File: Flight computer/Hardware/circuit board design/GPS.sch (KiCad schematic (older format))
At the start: 5 parts, among them J6 Conn_Coaxial, U4 MAX-M8C

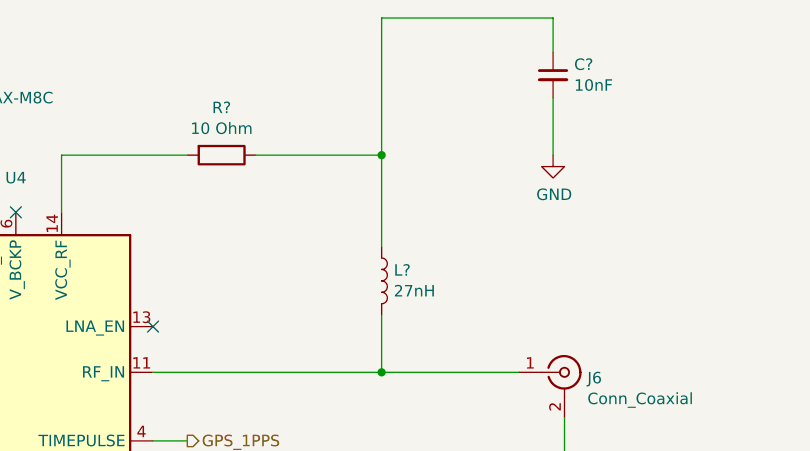
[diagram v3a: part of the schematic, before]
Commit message: fixed erc problems with Johanson integrated Frontend.
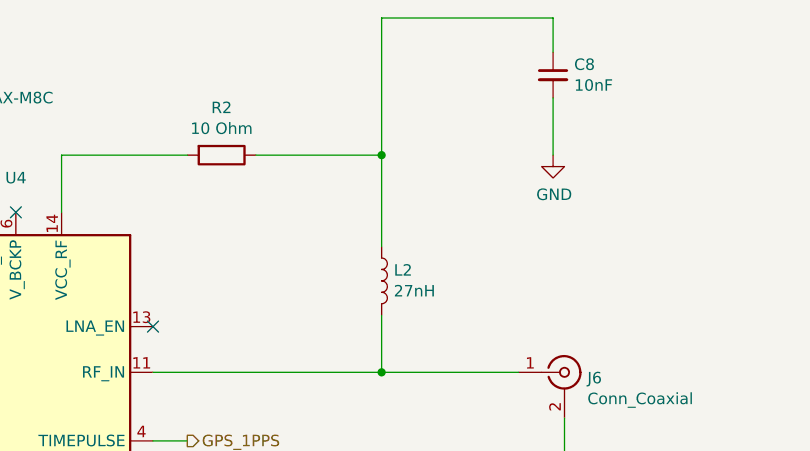
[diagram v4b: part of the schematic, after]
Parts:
- gave numbers to parts that had none: 3
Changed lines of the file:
@@
 	8450 4800 8450 4250
 $Comp
-L power:GND #PWR?
+L power:GND #PWR0114
 U 1 1 5D7B7248
 P 8450 4800
-F 0 "#PWR?" H 8450 4550 50  0001 C CNN
+F 0 "#PWR0114" H 8450 4550 50  0001 C CNN
 F 1 "GND" H 8455 4627 50  0000 C CNN
 F 2 "" H 8450 4800 50  0001 C CNN
@@
 	7650 4050 8250 4050
 $Comp
-L Device:L L?
+L Device:L L2
 U 1 1 5D7B7FB8
 P 7650 3650
-F 0 "L?" H 7703 3696 50  0000 L CNN
+F 0 "L2" H 7703 3696 50  0000 L CNN
 F 1 "27nH" H 7703 3605 50  0000 L CNN
 F 2 "" H 7650 3650 50  0001 C CNN
@@
 	7650 3100 7650 3500
 $Comp
-L Device:R R?
+L Device:R R2
 U 1 1 5D7B91DB
 P 6950 3100
-F 0 "R?" V 6743 3100 50  0000 C CNN
+F 0 "R2" V 6743 3100 50  0000 C CNN
 F 1 "10 Ohm" V 6834 3100 50  0000 C CNN
 F 2 "" V 6880 3100 50  0001 C CNN
@@
 Connection ~ 7650 3100
 $Comp
-L power:GND #PWR?
+L power:GND #PWR0116
 U 1 1 5D7B9CCD
 P 8400 3100
-F 0 "#PWR?" H 8400 2850 50  0001 C CNN
+F 0 "#PWR0116" H 8400 2850 50  0001 C CNN
 F 1 "GND" H 8405 2927 50  0000 C CNN
 F 2 "" H 8400 3100 50  0001 C CNN
@@
 	7650 2500 8400 2500
 $Comp
-L Device:C_Small C?
+L Device:C_Small C8
 U 1 1 5D7BADC4
 P 8400 2750
-F 0 "C?" H 8492 2796 50  0000 L CNN
+F 0 "C8" H 8492 2796 50  0000 L CNN
 F 1 "10nF" H 8492 2705 50  0000 L CNN
 F 2 "" H 8400 2750 50  0001 C CNN

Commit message: added in some comments
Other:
- note added: "Arrangement for Active antenna\n"
- note added: "Connected to active antenna, likely 2066400001 \nMolex active antenna. UFL connector\n"
- note removed: "Arranged according to Figure 7 in the MAX-8 / MAX-M8 u-blox 8 / M8 GNSS modules Hardware Integration Manual. Page 12."
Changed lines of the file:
@@
 Sheet 3 7
 Title ""
-Date ""
-Rev ""
-Comp ""
+Date "2019-09-09"
+Rev "1.0"
+Comp "Imperial College Space Society"
 Comment1 ""
 Comment2 ""
@@
 GPS_1PPS
 Text Notes 3000 5800 0    50   ~ 0
-Arranged according to Figure 7 in the MAX-8 / MAX-M8 u-blox 8 / M8 GNSS modules Hardware Integration Manual. Page 12.
-Text Notes 7550 5250 0    50   ~ 0
+Arrangement for Active antenna\n
+Text Notes 3800 6200 0    50   ~ 0
 http://www.explorelabs.com/blog/designing-a-gps-receiver/#ref-ublox-datasheet\n\nImportant info on why we use the components\n
 $Comp
@@
 Wire Wire Line
 	8400 2850 8400 3100
+Text Notes 8200 3850 0    50   ~ 0
+Connected to active antenna, likely 2066400001 \nMolex active antenna. UFL connector\n
 $EndSCHEMATC

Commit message: completed the pi circuit for Telemetry antenna
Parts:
- C8: footprint (none) -> Capacitor_SMD:C_0402_1005Metric
- L2, R2: footprint (none) -> Resistor_SMD:R_0402_1005Metric
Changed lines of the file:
@@
 F 0 "L2" H 7703 3696 50  0000 L CNN
 F 1 "27nH" H 7703 3605 50  0000 L CNN
-F 2 "" H 7650 3650 50  0001 C CNN
+F 2 "Resistor_SMD:R_0402_1005Metric" H 7650 3650 50  0001 C CNN
 F 3 "~" H 7650 3650 50  0001 C CNN
 	1    7650 3650
@@
 F 0 "R2" V 6743 3100 50  0000 C CNN
 F 1 "10 Ohm" V 6834 3100 50  0000 C CNN
-F 2 "" V 6880 3100 50  0001 C CNN
+F 2 "Resistor_SMD:R_0402_1005Metric" V 6880 3100 50  0001 C CNN
 F 3 "~" H 6950 3100 50  0001 C CNN
 	1    6950 3100
@@
 F 0 "C8" H 8492 2796 50  0000 L CNN
 F 1 "10nF" H 8492 2705 50  0000 L CNN
-F 2 "" H 8400 2750 50  0001 C CNN
+F 2 "Capacitor_SMD:C_0402_1005Metric" H 8400 2750 50  0001 C CNN
 F 3 "~" H 8400 2750 50  0001 C CNN
 	1    8400 2750

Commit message: added in comment about where I got the ref layout for GPS+active antenna
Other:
- note added: "Layout according to MAX-8 / MAX-M8, \nHardware Integration Manual,\nSection 2.4.2 Antenna design with active antenna."
- note removed: "Arrangement for Active antenna\n"
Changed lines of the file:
@@
 Text HLabel 6800 4350 2    50   Output ~ 0
 GPS_1PPS
-Text Notes 3000 5800 0    50   ~ 0
-Arrangement for Active antenna\n
 Text Notes 3800 6200 0    50   ~ 0
 http://www.explorelabs.com/blog/designing-a-gps-receiver/#ref-ublox-datasheet\n\nImportant info on why we use the components\n
@@
 Wire Wire Line
 	8400 2850 8400 3100
-Text Notes 8200 3850 0    50   ~ 0
+Text Notes 7500 5350 0    50   ~ 0
 Connected to active antenna, likely 2066400001 \nMolex active antenna. UFL connector\n
+Text Notes 5100 2400 0    50   ~ 0
+Layout according to MAX-8 / MAX-M8, \nHardware Integration Manual,\nSection 2.4.2 Antenna design with active antenna.
 $EndSCHEMATC

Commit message: tried routing first round
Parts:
- added C11: 100nF, Capacitor_SMD:C_0603_1608Metric, symbol Device:C_Small
- added C12: 2u2F, Capacitor_SMD:C_0603_1608Metric, symbol Device:C_Small
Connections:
- net +3V3: now also C11.1, C12.1
- net GND: now also C11.2, C12.2
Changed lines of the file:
@@
 http://www.explorelabs.com/blog/designing-a-gps-receiver/#ref-ublox-datasheet\n\nImportant info on why we use the components\n
-$Comp
-L power:+3.3V #PWR010
-U 1 1 5D692740
-P 5850 3150
-F 0 "#PWR010" H 5850 3000 50  0001 C CNN
-F 1 "+3.3V" H 5865 3323 50  0000 C CNN
-F 2 "" H 5850 3150 50  0001 C CNN
-F 3 "" H 5850 3150 50  0001 C CNN
-	1    5850 3150
-	1    0    0    -1
-$EndComp
 $Comp
 L power:GND #PWR011
@@
 	1    0    0    -1
 $EndComp
-Wire Wire Line
-	5850 3150 5850 3250
-Wire Wire Line
-	5950 3250 5850 3250
 Text HLabel 5150 3750 0    50   Output ~ 0
 GPS_TXD
@@
 Wire Wire Line
 	7650 3800 7650 4050
-Connection ~ 5850 3250
-Wire Wire Line
-	5150 4450 5450 4450
-Wire Wire Line
-	5850 3250 5850 3350
-Wire Wire Line
-	5950 3350 5950 3250
-NoConn ~ 6050 3350
-NoConn ~ 5450 4250
-Wire Wire Line
-	6650 4350 6800 4350
-Wire Wire Line
-	5450 3650 5150 3650
-Wire Wire Line
-	5150 3750 5450 3750
-Wire Wire Line
-	5450 4350 5150 4350
-Wire Wire Line
-	5150 4050 5450 4050
-Wire Wire Line
-	5450 3950 5150 3950
-NoConn ~ 6650 3850
-Wire Wire Line
-	6650 4050 7650 4050
-Wire Wire Line
-	6050 4750 6050 4900
-$Comp
-L RF_GPS:MAX-M8C U4
-U 1 1 5D610F77
-P 6050 4050
-F 0 "U4" H 6050 4900 50  0000 C CNN
-F 1 "MAX-M8C" H 6050 5250 50  0000 C CNN
-F 2 "RF_GPS:ublox_MAX" H 6450 3400 50  0001 C CNN
-F 3 "https://www.u-blox.com/sites/default/files/MAX-M8-FW3_DataSheet_%28UBX-15031506%29.pdf" H 6050 4050 50  0001 C CNN
-F 4 "11.99" H 6050 4050 50  0001 C CNN "Cost"
-F 5 "https://store.uputronics.com/index.php?route=product/product&product_id=71&search=ublox" H 6050 4050 50  0001 C CNN "Purchase link"
-	1    6050 4050
-	1    0    0    -1
-$EndComp
-Wire Wire Line
-	6250 3350 6250 3100
 Wire Wire Line
 	6250 3100 6800 3100
@@
 Text Notes 7500 5350 0    50   ~ 0
 Connected to active antenna, likely 2066400001 \nMolex active antenna. UFL connector\n
-Text Notes 5100 2400 0    50   ~ 0
+Text Notes 7000 1150 0    50   ~ 0
 Layout according to MAX-8 / MAX-M8, \nHardware Integration Manual,\nSection 2.4.2 Antenna design with active antenna.
+NoConn ~ 6050 3350
+NoConn ~ 5450 4250
+Wire Wire Line
+	6650 4350 6800 4350
+Wire Wire Line
+	6250 3350 6250 3100
+NoConn ~ 6650 3850
+Wire Wire Line
+	6650 4050 7650 4050
+Wire Wire Line
+	6050 4750 6050 4900
+Wire Wire Line
+	5950 3350 5950 2650
+Wire Wire Line
+	5850 2650 5850 3350
+Connection ~ 5850 2650
+Wire Wire Line
+	5950 2650 5850 2650
+Wire Wire Line
+	5850 2100 5850 2650
+$Comp
+L power:+3.3V #PWR010
+U 1 1 5D692740
+P 5850 2100
+F 0 "#PWR010" H 5850 1950 50  0001 C CNN
+F 1 "+3.3V" H 5865 2273 50  0000 C CNN
+F 2 "" H 5850 2100 50  0001 C CNN
+F 3 "" H 5850 2100 50  0001 C CNN
+	1    5850 2100
+	1    0    0    -1
+$EndComp
+Wire Wire Line
+	5300 3050 5300 2950
+Wire Wire Line
+	5650 2950 5650 3050
+Wire Wire Line
+	5650 2650 5300 2650
+Connection ~ 5650 2650
+Wire Wire Line
+	5650 2750 5650 2650
+Wire Wire Line
+	5300 2650 5300 2750
+Wire Wire Line
+	5850 2650 5650 2650
+$Comp
+L Device:C_Small C?
+U 1 1 5D99D571
+P 5300 2850
+AR Path="/5D5B17D8/5D99D571" Ref="C?"  Part="1"
+AR Path="/5D5B165E/5D99D571" Ref="C11"  Part="1"
+F 0 "C11" H 5208 2896 50  0000 R CNN
+F 1 "100nF" H 5208 2805 50  0000 R CNN
+F 2 "Capacitor_SMD:C_0603_1608Metric" H 5300 2850 50  0001 C CNN
+F 3 "~" H 5300 2850 50  0001 C CNN
+	1    5300 2850
+	1    0    0    -1
+$EndComp
+$Comp
+L Device:C_Small C?
+U 1 1 5D99D56B
+P 5650 2850
+AR Path="/5D5B17D8/5D99D56B" Ref="C?"  Part="1"
+AR Path="/5D5B165E/5D99D56B" Ref="C12"  Part="1"
+F 0 "C12" H 5558 2896 50  0000 R CNN
+F 1 "2u2F" H 5558 2805 50  0000 R CNN
+F 2 "Capacitor_SMD:C_0603_1608Metric" H 5650 2850 50  0001 C CNN
+F 3 "~" H 5650 2850 50  0001 C CNN
+	1    5650 2850
+	1    0    0    -1
+$EndComp
+Wire Wire Line
+	5150 4450 5450 4450
+Wire Wire Line
+	5450 4350 5150 4350
+Wire Wire Line
+	5150 4050 5450 4050
+Wire Wire Line
+	5450 3950 5150 3950
+Wire Wire Line
+	5150 3750 5450 3750
+Wire Wire Line
+	5450 3650 5150 3650
+$Comp
+L power:GND #PWR?
+U 1 1 5D99D57F
+P 5300 3150
+AR Path="/5D5B17D8/5D99D57F" Ref="#PWR?"  Part="1"
+AR Path="/5D5B165E/5D99D57F" Ref="#PWR029"  Part="1"
+F 0 "#PWR029" H 5300 2900 50  0001 C CNN
+F 1 "GND" H 5305 2977 50  0000 C CNN
+F 2 "" H 5300 3150 50  0001 C CNN
+F 3 "" H 5300 3150 50  0001 C CNN
+	1    5300 3150
+	1    0    0    -1
+$EndComp
+Wire Wire Line
+	5300 3150 5300 3050
+$Comp
+L RF_GPS:MAX-M8C U4
+U 1 1 5D610F77
+P 6050 4050
+F 0 "U4" H 6050 4900 50  0000 C CNN
+F 1 "MAX-M8C" H 6500 3300 50  0000 C CNN
+F 2 "RF_GPS:ublox_MAX" H 6450 3400 50  0001 C CNN
+F 3 "https://www.u-blox.com/sites/default/files/MAX-M8-FW3_DataSheet_%28UBX-15031506%29.pdf" H 6050 4050 50  0001 C CNN
+F 4 "11.99" H 6050 4050 50  0001 C CNN "Cost"
+F 5 "https://store.uputronics.com/index.php?route=product/product&product_id=71&search=ublox" H 6050 4050 50  0001 C CNN "Purchase link"
+	1    6050 4050
+	1    0    0    -1
+$EndComp
+Connection ~ 5300 3050
+Wire Wire Line
+	5300 3050 5650 3050
 $EndSCHEMATC
